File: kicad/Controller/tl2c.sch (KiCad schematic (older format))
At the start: 35 parts, among them IC101 ATTINY20-X, P101 12VDC, P102 I2C Master, P103 Spare, P104 TPI Header, P105 LED_DRIVER, P106 240VAC, P107 LED_DRIVER, P108 LED_OUT, P109 5VDC, SW101 TL3315NF160Q

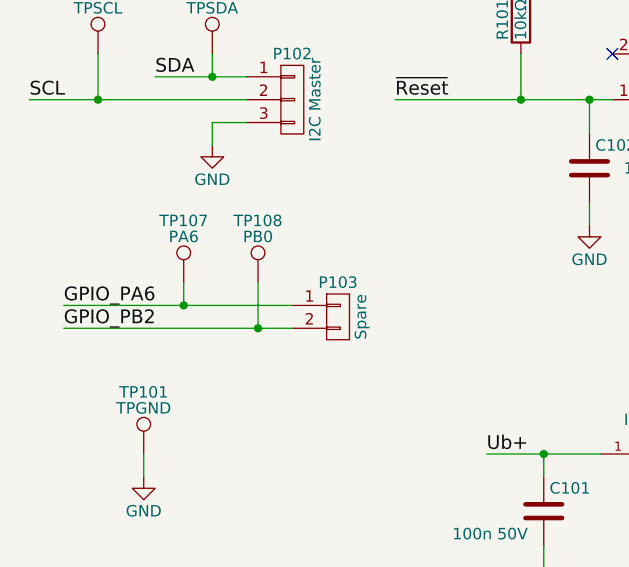
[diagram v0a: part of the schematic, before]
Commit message: Small changes to the clearances
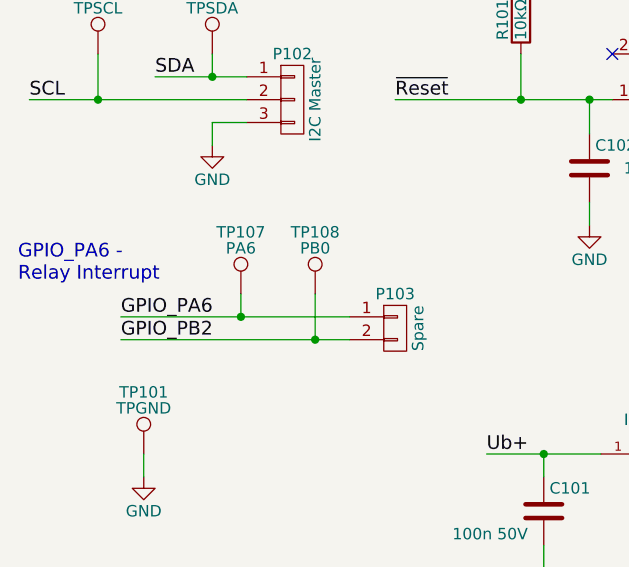
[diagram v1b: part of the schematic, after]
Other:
- note added: "GPIO_PA6 -\nRelay Interrupt"
- moved on the sheet: P103, TP107, TP108
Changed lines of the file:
@@
 L CONN_01X02 P103
 U 1 1 584CC850
-P 1950 4000
-F 0 "P103" H 1950 4150 50  0000 C CNN
-F 1 "Spare" V 2050 4000 50  0000 C CNN
-F 2 "Pin_Headers:Pin_Header_Straight_1x02" H 1950 4000 50  0001 C CNN
-F 3 "" H 1950 4000 50  0000 C CNN
-F 4 "Value" H 1950 4000 60  0001 C CNN "MFP"
-F 5 "Value" H 1950 4000 60  0001 C CNN "Conrad-PN"
-F 6 "Value" H 1950 4000 60  0001 C CNN "Digikey-PN"
-	1    1950 4000
+P 2200 4050
+F 0 "P103" H 2200 4200 50  0000 C CNN
+F 1 "Spare" V 2300 4050 50  0000 C CNN
+F 2 "Pin_Headers:Pin_Header_Straight_1x02" H 2200 4050 50  0001 C CNN
+F 3 "" H 2200 4050 50  0000 C CNN
+F 4 "Value" H 2200 4050 60  0001 C CNN "MFP"
+F 5 "Value" H 2200 4050 60  0001 C CNN "Conrad-PN"
+F 6 "Value" H 2200 4050 60  0001 C CNN "Digikey-PN"
+	1    2200 4050
 	1    0    0    -1
 $EndComp
@@
 Text Label 5400 3150 0    60   ~ 0
 GPIO_PB2
-Text Label 750  3950 0    60   ~ 0
+Text Label 1000 4000 0    60   ~ 0
 GPIO_PA6
-Text Label 750  4050 0    60   ~ 0
+Text Label 1000 4100 0    60   ~ 0
 GPIO_PB2
 $Comp
@@
 L TEST_1P TP107
 U 1 1 586D80EA
-P 1275 3850
-F 0 "TP107" H 1275 4120 50  0000 C CNN
-F 1 "PA6" H 1275 4050 50  0000 C CNN
-F 2 "Measurement_Points:Measurement_Point_Round-SMD-Pad_Small" H 1475 3850 50  0001 C CNN
-F 3 "" H 1475 3850 50  0000 C CNN
-	1    1275 3850
+P 1525 3900
+F 0 "TP107" H 1525 4170 50  0000 C CNN
+F 1 "PA6" H 1525 4100 50  0000 C CNN
+F 2 "Measurement_Points:Measurement_Point_Round-SMD-Pad_Small" H 1725 3900 50  0001 C CNN
+F 3 "" H 1725 3900 50  0000 C CNN
+	1    1525 3900
 	1    0    0    -1
 $EndComp
@@
 L TEST_1P TP108
 U 1 1 586D81E0
-P 1600 3850
-F 0 "TP108" H 1600 4120 50  0000 C CNN
-F 1 "PB0" H 1600 4050 50  0000 C CNN
-F 2 "Measurement_Points:Measurement_Point_Round-SMD-Pad_Small" H 1800 3850 50  0001 C CNN
-F 3 "" H 1800 3850 50  0000 C CNN
-	1    1600 3850
+P 1850 3900
+F 0 "TP108" H 1850 4170 50  0000 C CNN
+F 1 "PB0" H 1850 4100 50  0000 C CNN
+F 2 "Measurement_Points:Measurement_Point_Round-SMD-Pad_Small" H 2050 3900 50  0001 C CNN
+F 3 "" H 2050 3900 50  0000 C CNN
+	1    1850 3900
 	1    0    0    -1
 $EndComp
@@
 	10000 1250 9625 1250
 Wire Wire Line
-	750  3950 1750 3950
-Wire Wire Line
-	750  4050 1750 4050
+	1000 4000 2000 4000
+Wire Wire Line
+	1000 4100 2000 4100
 Wire Wire Line
 	3650 3050 3850 3050
@@
 	7575 3350 7575 3600
 Wire Wire Line
-	1275 3850 1275 3950
-Connection ~ 1275 3950
-Wire Wire Line
-	1600 3850 1600 4050
-Connection ~ 1600 4050
+	1525 3900 1525 4000
+Connection ~ 1525 4000
+Wire Wire Line
+	1850 3900 1850 4100
+Connection ~ 1850 4100
 Wire Wire Line
 	7475 2650 9000 2650
@@
 Text Label 3850 1200 0    60   ~ 0
 TPICLK
+Text Notes 550  3850 0    60   ~ 0
+GPIO_PA6 -\nRelay Interrupt
 $EndSCHEMATC
